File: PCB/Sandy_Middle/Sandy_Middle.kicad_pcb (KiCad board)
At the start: 2 copper layers, 285 x 73.4 mm, 71 parts, among them J1 Conn_02x02_Top_Bottom, J2 Conn_02x02_Top_Bottom, J3 Conn_02x02_Top_Bottom

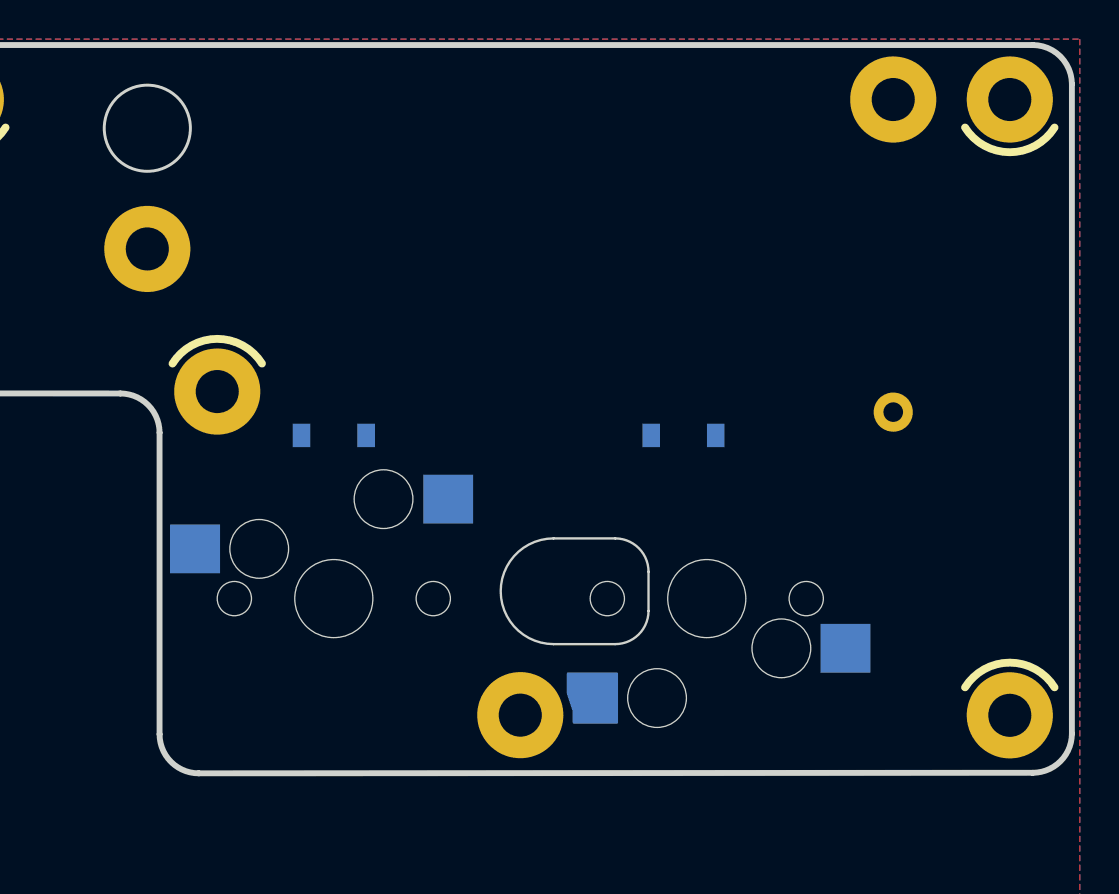
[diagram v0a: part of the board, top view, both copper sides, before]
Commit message: 位置合わせガイドを削除
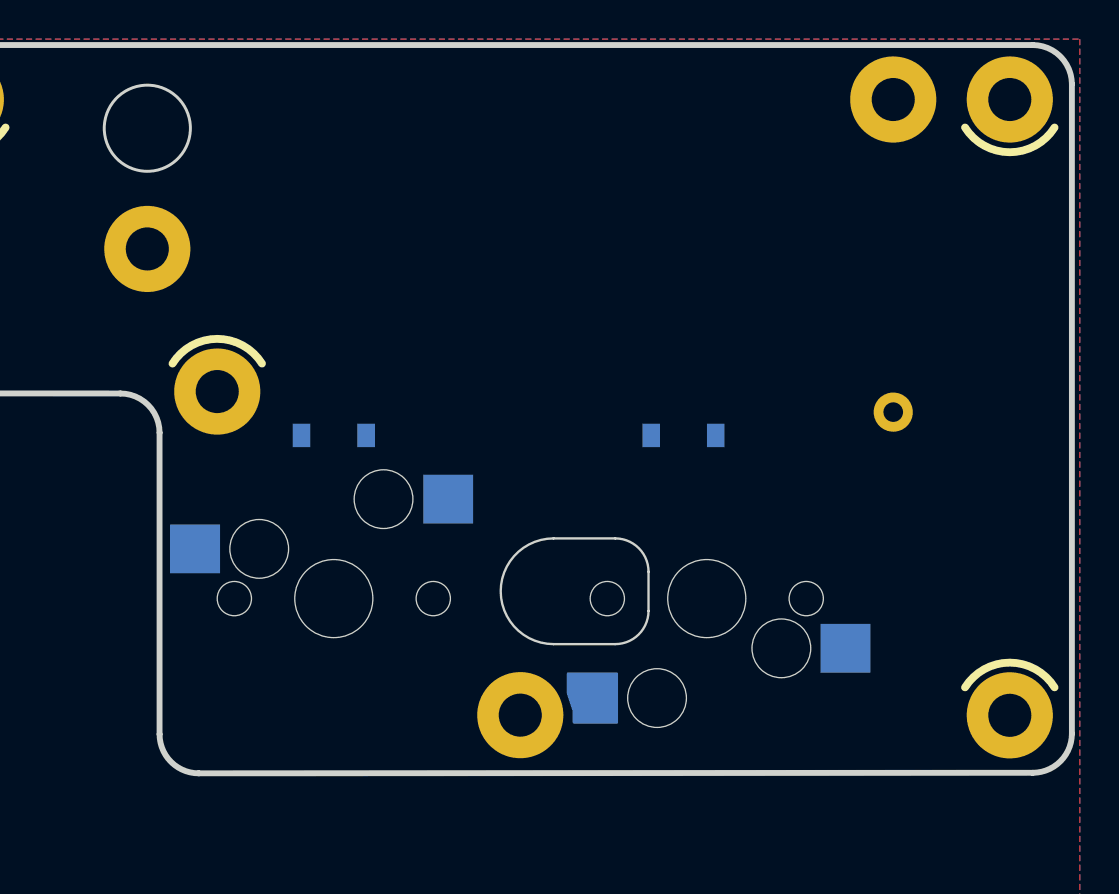
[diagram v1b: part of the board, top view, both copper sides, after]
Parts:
- removed REF**: 60_Outline, locallib:60_Outline-Sandy-DN0040-Top-NoSwImage-WithHole2-ECO1

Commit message: WIP 配線中。ハンダマスクの拡張を変更0.2→0
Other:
- rule pad_to_mask_clearance: 0.2 -> 0
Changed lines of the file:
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@@
 			(dielectric_constraints no)
 		)
-		(pad_to_mask_clearance 0.2)
+		(pad_to_mask_clearance 0)
 		(allow_soldermask_bridges_in_footprints no)
 		(aux_axis_origin 21.058435 21.05028)
@@
 		(fp_arc
 			(start 114.175 -9.90004)
-			(mid 114.731482 -11.243546)
+			(mid 114.731476 -11.243582)
 			(end 116.075 -11.80004)
 			(stroke
@@
 		(fp_arc
 			(start 114.923491 -9.898554)
-			(mid 115.274981 -10.74705)
+			(mid 115.274975 -10.747086)
 			(end 116.123491 -11.098554)
 			(stroke
@@
 		(fp_arc
 			(start 116.075 -8.00004)
-			(mid 114.731447 -8.556504)
+			(mid 114.731482 -8.55651)
 			(end 114.175 -9.90004)
 			(stroke
@@
 		(fp_arc
 			(start 116.123491 -8.698554)
-			(mid 115.275017 -9.050062)
+			(mid 115.274982 -9.050056)
 			(end 114.923491 -9.898554)
 			(stroke
@@
 		(fp_arc
 			(start 118.923491 -11.098554)
-			(mid 119.772073 -10.747118)
+			(mid 119.772038 -10.747112)
 			(end 120.123491 -9.898554)
 			(stroke
@@
 		(fp_arc
 			(start 118.975 -11.80004)
-			(mid 120.318452 -11.24351)
+			(mid 120.318488 -11.243516)
 			(end 120.875 -9.90004)
 			(stroke
@@
 		(fp_arc
 			(start 120.123491 -9.898554)
-			(mid 119.772038 -9.049994)
+			(mid 119.772032 -9.050029)
 			(end 118.923491 -8.698554)
 			(stroke
@@
 		(fp_arc
 			(start 120.875 -9.90004)
-			(mid 120.318488 -8.556541)
+			(mid 120.318482 -8.556576)
 			(end 118.975 -8.00004)
 			(stroke
@@
 		(fp_arc
 			(start 14.2875 -4.762415)
-			(mid 14.984924 -6.446239)
+			(mid 14.984924 -6.446243)
 			(end 16.66875 -7.143665)
 			(stroke
@@
 		(fp_arc
 			(start 14.2875 -1.190583)
-			(mid 13.590054 0.493219)
+			(mid 13.590051 0.493216)
 			(end 11.90625 1.190667)
 			(stroke
@@
 		(fp_arc
 			(start 27.384375 -28.575)
-			(mid 29.068164 -27.87754)
+			(mid 29.068167 -27.877541)
 			(end 29.765625 -26.19375)
 			(stroke
@@
 		(fp_arc
 			(start 27.975 33.570786)
-			(mid 27.389238 34.985022)
+			(mid 27.389238 34.985026)
 			(end 25.975 35.570786)
 			(stroke
@@
 		(fp_arc
 			(start 93.875 -20.001612)
-			(mid 95.289182 -19.41582)
+			(mid 95.289189 -19.415797)
 			(end 95.875 -18.001612)
 			(stroke
@@
 		(fp_arc
 			(start 97.875 -0.60004)
-			(mid 96.460736 -1.185794)
+			(mid 96.460771 -1.1858)
 			(end 95.875 -2.60004)
 			(stroke
@@
 		(fp_arc
 			(start 140.475 -37.80004)
-			(mid 141.889163 -37.214221)
+			(mid 141.889198 -37.214227)
 			(end 142.475 -35.80004)
 			(stroke
@@
 		(fp_arc
 			(start 142.475 -2.628468)
-			(mid 141.889238 -1.21421)
+			(mid 141.889232 -1.214246)
 			(end 140.475 -0.628468)
 			(stroke

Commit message: WIP 配線調整
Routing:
- net Mid_row6: track 0.00 -> 337.0 mm, vias 0 -> 9
- net Mid_row1: track 0.00 -> 301.2 mm, vias 0 -> 4
- net Mid_col0: track 0.00 -> 231.5 mm, vias 0 -> 1
- net Mid_col6: track 0.00 -> 173.8 mm, vias 0 -> 5
- net Mid_col3: track 0.00 -> 149.5 mm, vias 0 -> 3
- net Mid_col4: track 0.00 -> 114.1 mm, vias 0 -> 3
- net Mid_col2: track 0.00 -> 106.6 mm, vias 0 -> 3
- net Mid_row2: track 0.00 -> 104.9 mm, vias 0 -> 3
- net Mid_row7: track 0.00 -> 89.1 mm, vias 0 -> 1
- net Mid_row3: track 0.00 -> 83.9 mm, vias 0 -> 1
- net Mid_row8: track 0.00 -> 78.8 mm
- net Mid_row0: track 0.00 -> 46.7 mm
- net Mid_row5: track 0.00 -> 44.2 mm
- net Net-(D6-A): track 0.00 -> 33.4 mm
- net Mid_col5: track 0.00 -> 20.1 mm
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
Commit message: パーツ・配線微調整。Mid一旦FIX
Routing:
- net Mid_row6: track 337.0 -> 341.2 mm, vias 9 -> 10
- net Mid_col5: track 20.1 -> 23.8 mm
- net Mid_row1: track 301.2 -> 298.9 mm
- net Mid_col6: track 173.8 -> 175.5 mm, vias 5 -> 6
- net Mid_GND: vias 0 -> 92

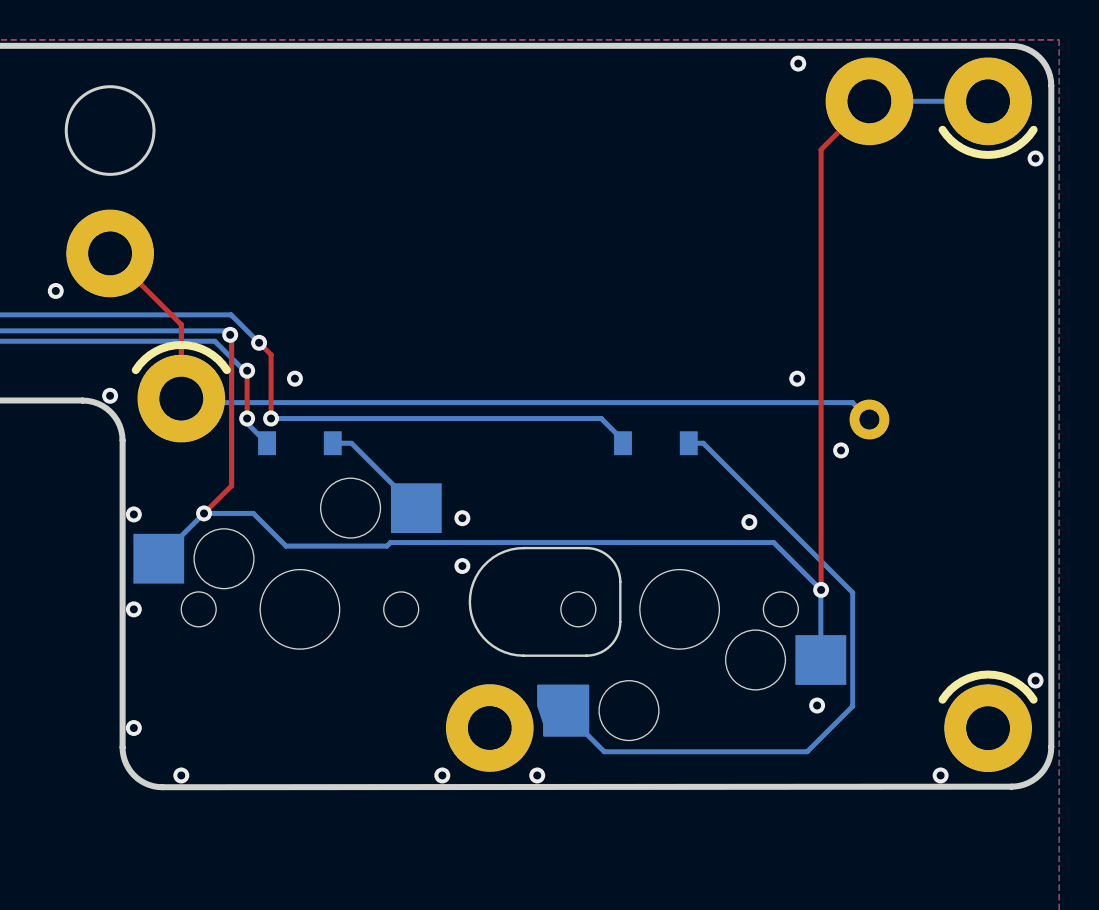
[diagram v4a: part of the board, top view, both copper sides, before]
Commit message: GNDとMid_GNDを接続
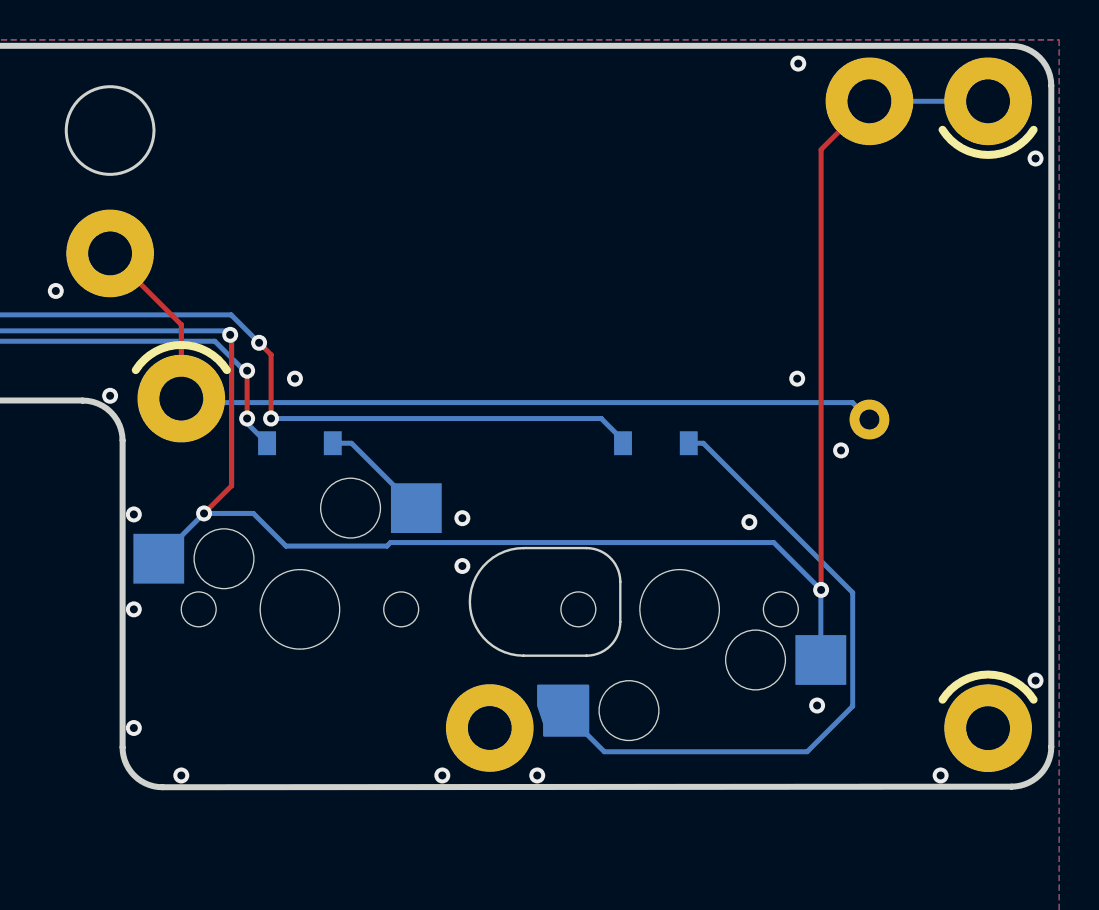
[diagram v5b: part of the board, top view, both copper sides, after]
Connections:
- J2 pad 4: GND -> Mid_GND
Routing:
- net Mid_GND: track 0.00 -> 2.01 mm
- net GND: track 2.01 -> 0.00 mm

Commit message: WIP Choc V2のフットプリントに変更。配置考え中。
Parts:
- SW_BS1: footprint MX_Alps_Hybrid:MXOnly-1U-Hotswap-screw-hole-side1-guide -> locallib:Kailh_socket_ChocV2
- SW_G1, SW_H1, SW_P1, SW_Q1, SW_R1, SW_R4CNT_C1, SW_R4CNT_L1, SW_R4CNT_R1, SW_TAB1, SW_U1: footprint MX_Alps_Hybrid:MXOnly-1U-Hotswap-guide -> locallib:Kailh_socket_ChocV2
- turned SW_BS1 to 0 degrees
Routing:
- net Mid_row6: track 341.2 -> 0.00 mm, vias 10 -> 0
- net Mid_row1: track 298.9 -> 0.00 mm, vias 4 -> 0
- net Mid_col0: track 231.5 -> 0.00 mm, vias 1 -> 0
- net Mid_col6: track 175.5 -> 0.00 mm, vias 6 -> 0
- net Mid_col3: track 149.5 -> 0.00 mm, vias 3 -> 0
- net Mid_col4: track 114.1 -> 0.00 mm, vias 3 -> 0
- net Mid_col2: track 106.6 -> 0.00 mm, vias 3 -> 0
- net Mid_row2: track 104.9 -> 0.00 mm, vias 3 -> 0
- net Mid_row7: track 89.1 -> 0.00 mm, vias 1 -> 0
- net Mid_row3: track 83.9 -> 0.00 mm, vias 1 -> 0
- net Mid_row8: track 78.8 -> 0.00 mm
- net Mid_row0: track 46.7 -> 0.00 mm
- net Mid_row5: track 43.7 -> 0.00 mm
- net Net-(D6-A): track 33.4 -> 0.00 mm
- net Mid_col5: track 23.8 -> 0.00 mm
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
